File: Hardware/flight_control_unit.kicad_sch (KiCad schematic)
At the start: 36 parts, among them SW3 SW_SPDT, SW4 SW_Push_Dual, U12 STM32F405RGTx, Y2 25MHz

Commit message: hardware version 0.1.2, minor improvements and footprint selection (missing some gnss and bulk regulator components
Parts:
- SW3: footprint (none) -> Button_Switch_SMD:SW_SPDT_PCM12
- SW4: footprint (none) -> Aircraft_Footprints:SW_SKRPACE010
- Y2: footprint (none) -> Crystal:Crystal_SMD_Abracon_ABM8G-4Pin_3.2x2.5mm
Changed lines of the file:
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@@
 	(title_block
 		(title "Flight Control Unit")
-		(rev "0.1.1")
+		(rev "0.1.2")
 		(company "Breno Soares Alves")
 	)
@@
 			)
 		)
-		(property "Footprint" ""
+		(property "Footprint" "Button_Switch_SMD:SW_SPDT_PCM12"
 			(at 186.69 104.14 0)
 			(effects
@@
 			)
 		)
-		(property "Footprint" ""
+		(property "Footprint" "Aircraft_Footprints:SW_SKRPACE010"
 			(at 238.76 87.63 0)
 			(effects
@@
 			)
 		)
-		(property "Footprint" ""
+		(property "Footprint" "Crystal:Crystal_SMD_Abracon_ABM8G-4Pin_3.2x2.5mm"
 			(at 157.48 64.77 0)
 			(effects

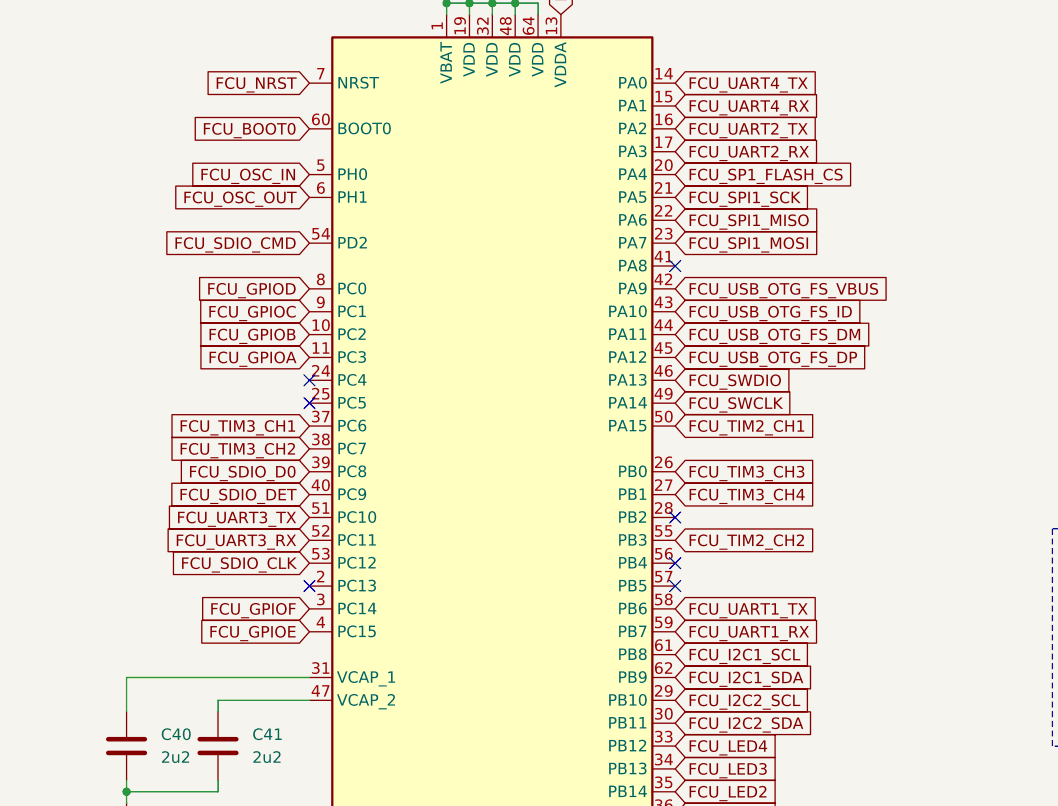
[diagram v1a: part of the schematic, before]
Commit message: board placement, no trails, just pain
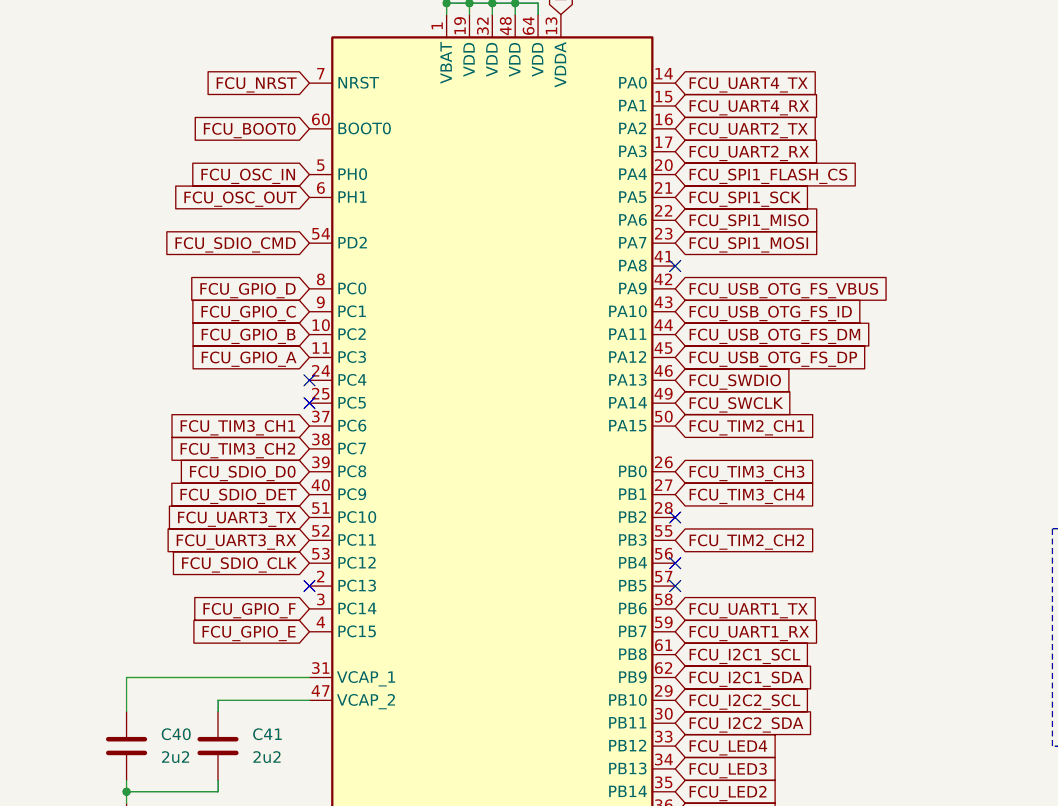
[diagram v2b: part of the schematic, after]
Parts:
- C40, C41: footprint Capacitor_SMD:C_0603_1608Metric -> Capacitor_SMD:C_0402_1005Metric; Digikey_Link (none) -> https://www.digikey.com.br/pt/products/detail/samsung-elect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; MPN (none) -> CL10B225KP8NNNC
- C42: footprint Capacitor_Tantalum_SMD:CP_EIA-1608-08_AVX-J -> Capacitor_SMD:C_1206_3216Metric_Pad1.33x1.80mm_HandSolder; Digikey_Link (none) -> https://www.digikey.com.br/pt/products/detail/kyocera-avx/T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; MPN (none) -> TAJA106K010TNJ
- C43, C46: Digikey_Link (none) -> https://www.digikey.com.br/pt/products/detail/w%C3%BCrth-el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; MPN (none) -> 885012005007
- C44, C45, C47, C48, C49, C50, C51, C52: Digikey_Link (none) -> https://www.digikey.com.br/pt/products/detail/samsung-elect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; MPN (none) -> CL05B104KP5NNNC
- C53: Digikey_Link (none) -> https://www.digikey.com.br/pt/products/detail/kemet/C0603C1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; MPN (none) -> C0603C104K8RACTU
- C54: Digikey_Link (none) -> https://www.digikey.com.br/pt/products/detail/kemet/T491A10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; MPN (none) -> T491A105K010AT
- D10: footprint LED_SMD:LED_0805_2012Metric -> LED_SMD:LED_0805_2012Metric_Pad1.15x1.40mm_HandSolder; Digikey_Link (none) -> https://www.digikey.com.br/pt/products/detail/liteon/LTST-C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; MPN (none) -> LTST-C171YKT
- D11: footprint LED_SMD:LED_0805_2012Metric -> LED_SMD:LED_0805_2012Metric_Pad1.15x1.40mm_HandSolder; Digikey_Link (none) -> https://www.digikey.com.br/pt/products/detail/liteon/LTST-C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; MPN (none) -> LTST-C171TBKT
- D8: footprint LED_SMD:LED_0805_2012Metric -> LED_SMD:LED_0805_2012Metric_Pad1.15x1.40mm_HandSolder; Digikey_Link (none) -> https://www.digikey.com.br/pt/products/detail/liteon/LTST-C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; MPN (none) -> LTST-C171KRKT
- D9: footprint LED_SMD:LED_0805_2012Metric -> LED_SMD:LED_0805_2012Metric_Pad1.15x1.40mm_HandSolder; Digikey_Link (none) -> https://www.digikey.com.br/pt/products/detail/liteon/LTST-C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; MPN (none) -> LTST-C170GKT
- FB2: footprint Inductor_SMD:L_0805_2012Metric -> Inductor_SMD:L_0805_2012Metric_Pad1.05x1.20mm_HandSolder; Digikey_Link (none) -> https://www.digikey.com.br/pt/products/detail/laird-signal-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; MPN (none) -> HZ0805E601R-10
- R23, R26, R27: Digikey_Link (none) -> https://www.digikey.com.br/pt/products/detail/yageo/RC0603J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; MPN (none) -> RC0603JR-07330RL
- R24: Digikey_Link (none) -> https://www.digikey.com.br/pt/products/detail/yageo/RC0603F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; MPN (none) -> RC0603FR-07620RL
- R25: Digikey_Link (none) -> https://www.digikey.com.br/pt/products/detail/yageo/RC0603F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; MPN (none) -> RC0603FR-0710KL
- R28: Digikey_Link (none) -> https://www.digikey.com.br/pt/products/detail/stackpole-ele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; MPN (none) -> RMCF0603FT560R
- R29, R30, R31, R32: Digikey_Link (none) -> https://www.digikey.com.br/pt/products/detail/panasonic-ele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; MPN (none) -> ERJ-3EKF4701V
- SW3: Digikey_Link (none) -> https://www.digikey.com.br/pt/products/detail/c-k/pcm12smtb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; MPN (none) -> PCM12SMTR
- SW4: footprint Aircraft_Footprints:SW_SKRPACE010 -> Aircraft_Footprints:SW4_PTS815 SJM 250 SMTR LFS_CNK; Digikey_Link (none) -> https://www.digikey.com.br/pt/products/detail/c-k/PTS815SJM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; MPN (none) -> PTS815SJM250SMTRLFS
- TP3, TP4: footprint TestPoint:TestPoint_Pad_D2.5mm -> TestPoint:TestPoint_Pad_D1.0mm; now left out of the parts list
- U12: Digikey_Link (none) -> https://www.digikey.com.br/pt/products/detail/stmicroelectr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; MPN (none) -> STM32F405RGT6
- Y2: Digikey_Link (none) -> https://www.digikey.com.br/pt/products/detail/abracon-llc/a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; MPN (none) -> ABM8G-25.000MHZ-B4Y-T3
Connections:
- net FCU_GPIOA renamed FCU_GPIO_A
- net FCU_GPIOB renamed FCU_GPIO_B
- net FCU_GPIOC renamed FCU_GPIO_C
- net FCU_GPIOD renamed FCU_GPIO_D
- net FCU_GPIOE renamed FCU_GPIO_E
- net FCU_GPIOF renamed FCU_GPIO_F
- net FCU_SP1_FLASH_CS renamed FCU_SPI1_FLASH_CS
